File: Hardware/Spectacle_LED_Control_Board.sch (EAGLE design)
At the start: 39 parts, among them J1 FTDI_DEVICE, J10 AUDIO-JACK3, J3 USB-MICROB, J4 AUDIO-JACK3, U1 CY8C4146LQI-S422, U2 3.3V/150mA

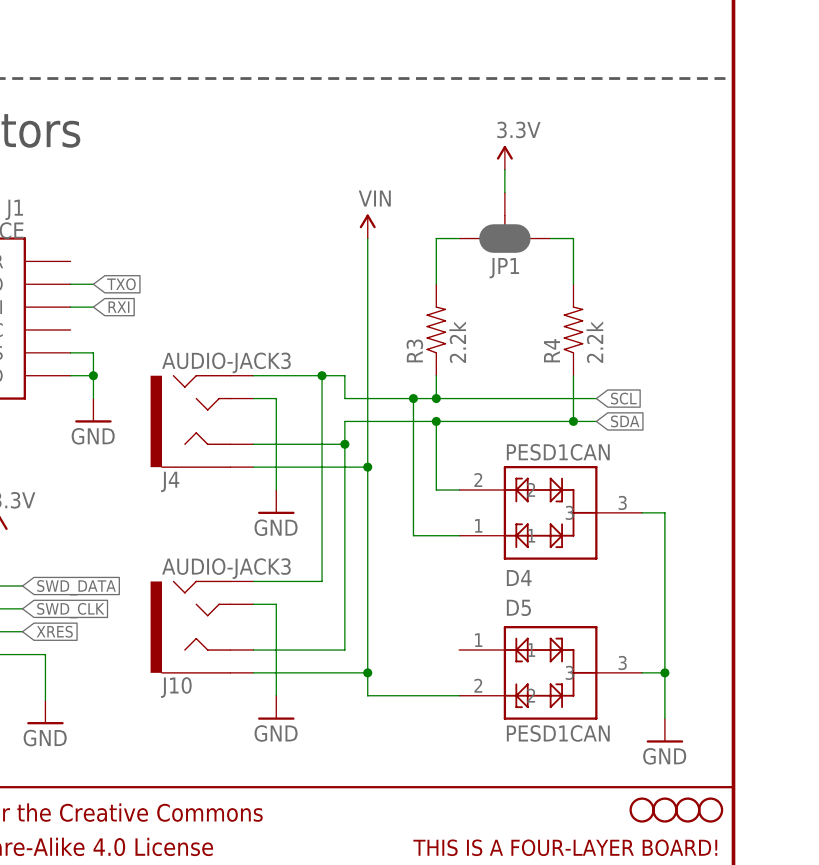
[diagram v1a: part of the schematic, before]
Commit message: QC edits, round one
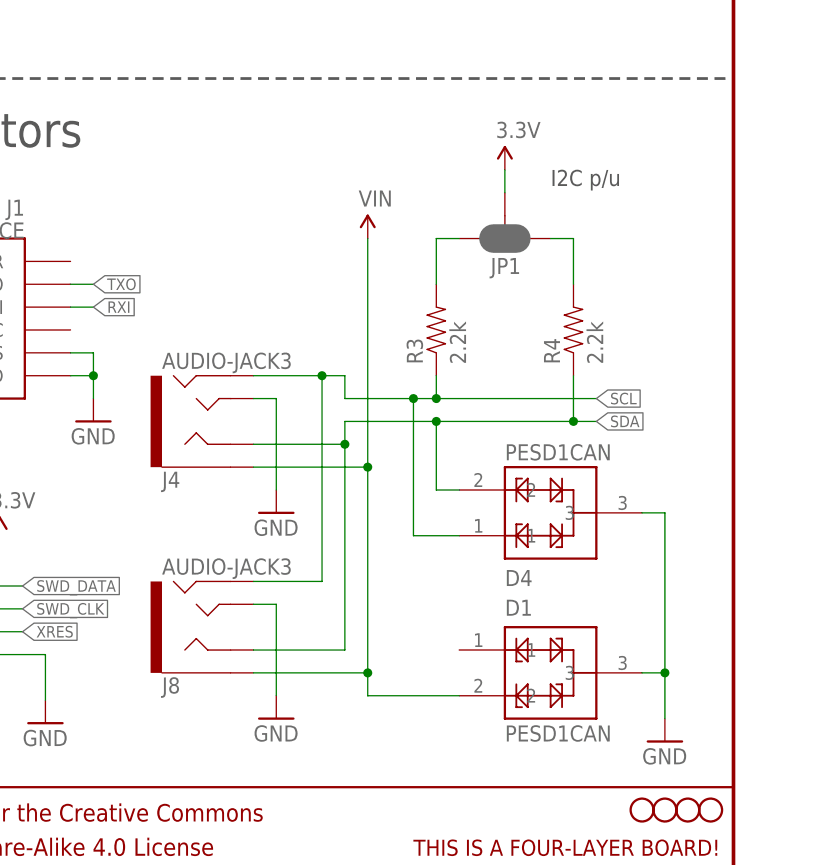
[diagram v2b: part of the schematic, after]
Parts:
- renumbered D5 to D1, J10 to J8
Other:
- note added: "I2C p/u"
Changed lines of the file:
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@@
 <?xml version="1.0" encoding="utf-8"?>
 <!DOCTYPE eagle SYSTEM "eagle.dtd">
-<eagle version="7.3.0">
+<eagle version="7.6.0">
 <drawing>
 <settings>
@@
 <part name="D4" library="SparkFun-DiscreteSemi" deviceset="PESD1CAN" device=""/>
 <part name="GND4" library="SparkFun-Aesthetics" deviceset="GND" device=""/>
-<part name="D5" library="SparkFun-DiscreteSemi" deviceset="PESD1CAN" device=""/>
+<part name="D1" library="SparkFun-DiscreteSemi" deviceset="PESD1CAN" device=""/>
 <part name="SUPPLY1" library="SparkFun-Aesthetics" deviceset="3.3V" device=""/>
 <part name="H1" library="SparkFun-Electromechanical" deviceset="STAND-OFF" device=""/>
@@
 <part name="LOGO1" library="SparkFun-Aesthetics" deviceset="OSHW-LOGO" device="S"/>
 <part name="LOGO2" library="SparkFun-Aesthetics" deviceset="SFE_LOGO_NAME_FLAME" device=".1_INCH"/>
-<part name="J10" library="SparkFun-Connectors" deviceset="AUDIO-JACK3" device=""/>
+<part name="J8" library="SparkFun-Connectors" deviceset="AUDIO-JACK3" device=""/>
 <part name="GND16" library="SparkFun-Aesthetics" deviceset="GND" device=""/>
 <part name="GND17" library="SparkFun-Aesthetics" deviceset="GND" device=""/>
@@
 Supply</text>
 <text x="4.318" y="88.9" size="2.54" layer="97" font="vector">4.5V &lt; VIN &lt; 5.5V</text>
+<text x="228.6" y="102.362" size="1.778" layer="97" font="vector">I2C p/u</text>
 </plain>
 <instances>
@@
 <instance part="D4" gate="G$1" x="223.52" y="71.12" rot="MR180"/>
 <instance part="GND4" gate="1" x="241.3" y="40.64"/>
-<instance part="D5" gate="G$1" x="223.52" y="43.18"/>
+<instance part="D1" gate="G$1" x="223.52" y="43.18"/>
 <instance part="SUPPLY1" gate="G$1" x="22.86" y="177.8"/>
 <instance part="H1" gate="G$1" x="246.38" y="33.02"/>
@@
 <instance part="LOGO1" gate="G$1" x="81.28" y="10.16"/>
 <instance part="LOGO2" gate="G$1" x="88.9" y="0"/>
-<instance part="J10" gate="G$1" x="190.5" y="53.34" rot="MR180"/>
+<instance part="J8" gate="G$1" x="190.5" y="53.34" rot="MR180"/>
 <instance part="GND16" gate="1" x="198.12" y="43.18"/>
 <instance part="GND17" gate="1" x="27.94" y="22.86"/>
@@
 <wire x1="238.76" y1="66.04" x2="241.3" y2="66.04" width="0.1524" layer="91"/>
 <wire x1="241.3" y1="66.04" x2="241.3" y2="48.26" width="0.1524" layer="91"/>
-<pinref part="D5" gate="G$1" pin="3"/>
+<pinref part="D1" gate="G$1" pin="3"/>
 <wire x1="241.3" y1="48.26" x2="241.3" y2="43.18" width="0.1524" layer="91"/>
 <wire x1="238.76" y1="48.26" x2="241.3" y2="48.26" width="0.1524" layer="91"/>
@@
 </segment>
 <segment>
-<pinref part="J10" gate="G$1" pin="TIP"/>
+<pinref part="J8" gate="G$1" pin="TIP"/>
 <pinref part="GND16" gate="1" pin="GND"/>
 <wire x1="195.58" y1="55.88" x2="198.12" y2="55.88" width="0.1524" layer="91"/>
@@
 <wire x1="208.28" y1="45.72" x2="208.28" y2="48.26" width="0.1524" layer="91"/>
 <junction x="208.28" y="71.12"/>
-<pinref part="D5" gate="G$1" pin="2"/>
+<pinref part="D1" gate="G$1" pin="2"/>
 <wire x1="208.28" y1="48.26" x2="208.28" y2="71.12" width="0.1524" layer="91"/>
 <wire x1="208.28" y1="45.72" x2="218.44" y2="45.72" width="0.1524" layer="91"/>
-<pinref part="J10" gate="G$1" pin="EARTH"/>
+<pinref part="J8" gate="G$1" pin="EARTH"/>
 <wire x1="195.58" y1="48.26" x2="208.28" y2="48.26" width="0.1524" layer="91"/>
 <junction x="208.28" y="48.26"/>
@@
 <pinref part="D4" gate="G$1" pin="1"/>
 <wire x1="218.44" y1="63.5" x2="213.36" y2="63.5" width="0.1524" layer="91"/>
-<pinref part="J10" gate="G$1" pin="RING2"/>
+<pinref part="J8" gate="G$1" pin="RING2"/>
 <wire x1="195.58" y1="58.42" x2="203.2" y2="58.42" width="0.1524" layer="91"/>
 <wire x1="203.2" y1="58.42" x2="203.2" y2="81.28" width="0.1524" layer="91"/>
@@
 <wire x1="205.74" y1="73.66" x2="205.74" y2="50.8" width="0.1524" layer="91"/>
 <junction x="205.74" y="73.66"/>
-<pinref part="J10" gate="G$1" pin="RING1"/>
+<pinref part="J8" gate="G$1" pin="RING1"/>
 <wire x1="205.74" y1="50.8" x2="195.58" y2="50.8" width="0.1524" layer="91"/>
 </segment>

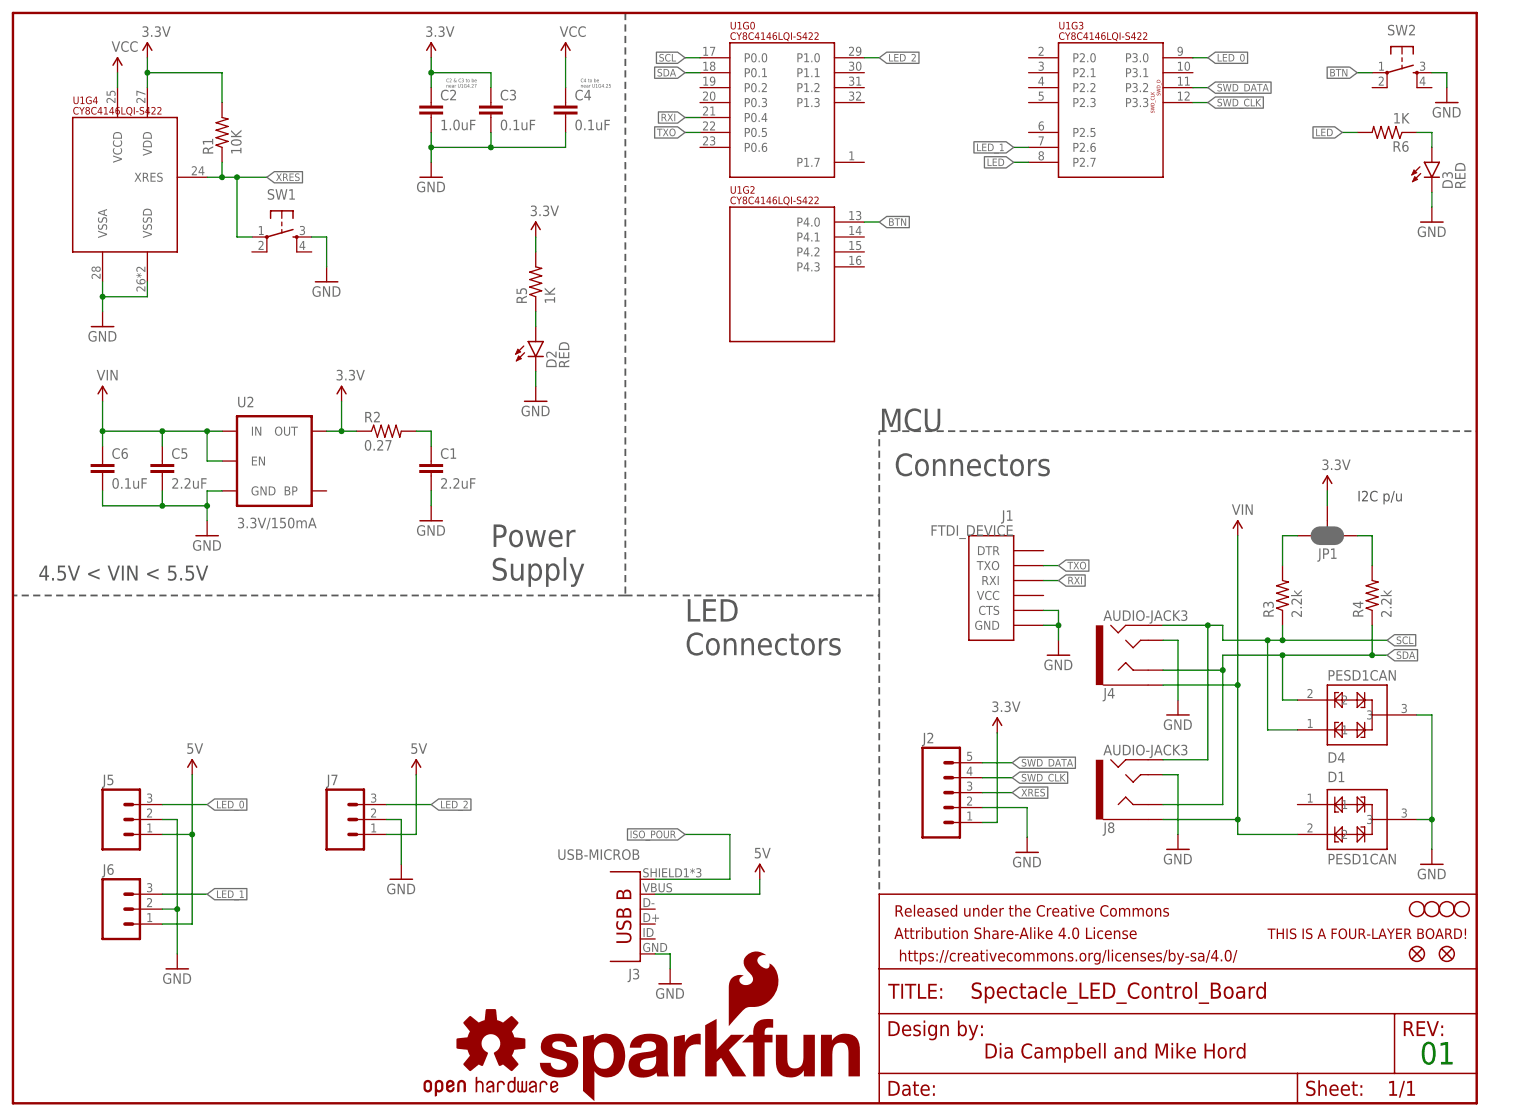
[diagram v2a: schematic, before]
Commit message: Added circuitry for downstream power control
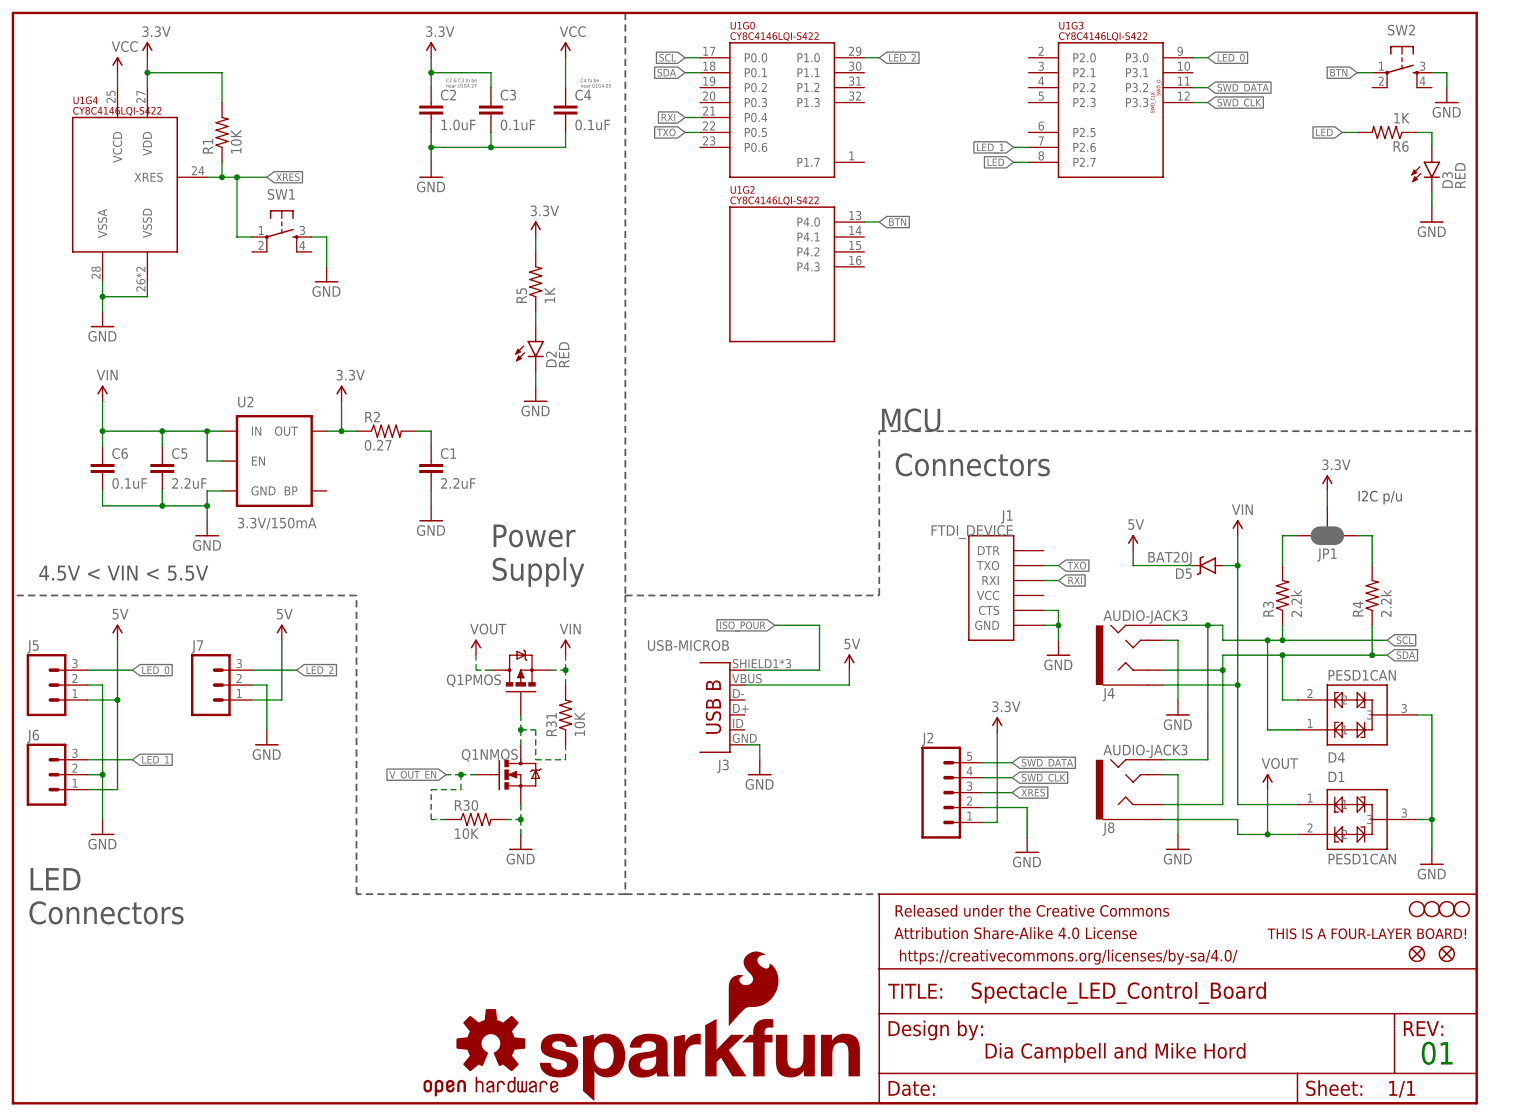
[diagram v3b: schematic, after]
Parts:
- added D5: BAT20J, SparkFun-DiscreteSemi:DIODE-SCHOTTKY-BAT20J
- added Q1: (no value), SparkFun-DiscreteSemi:IRF7509
- added R30, R31: 10K, SparkFun-Resistors:10KOHM-1/10W-1%(0603)0603
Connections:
- new net N$26: Q1NMOS.D, Q1PMOS.G, R31.1
- new net VOUT: D1.2, J8.EARTH, Q1PMOS.D
- new net V_OUT_EN: Q1NMOS.G, R30.1
- net 5V: now also D5.C
- net GND: now also Q1NMOS.S, R30.2
- net VIN: now also D1.1, D5.A, Q1PMOS.S, R31.2; no longer D1.2, J8.EARTH
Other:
- moved on the sheet: J3, J5, J6, J7

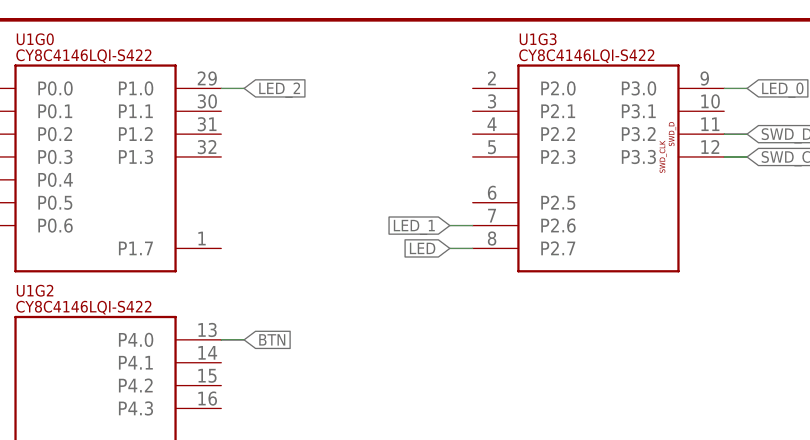
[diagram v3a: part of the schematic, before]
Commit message: Added enable pin
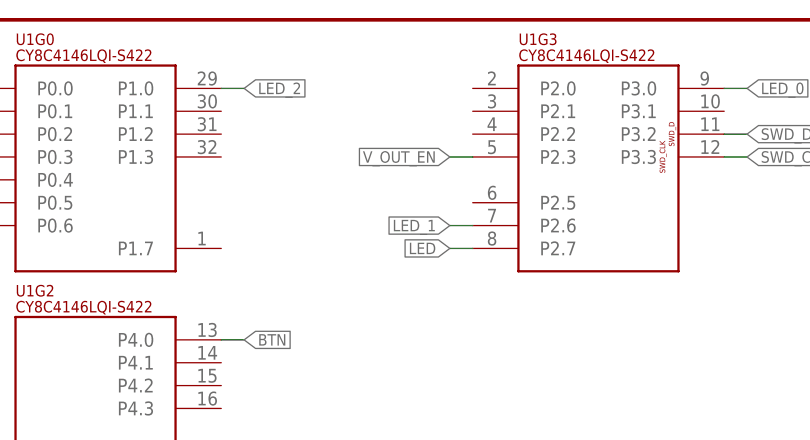
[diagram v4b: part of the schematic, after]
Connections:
- net V_OUT_EN: now also U1G3.P2.3
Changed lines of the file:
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@@
 <junction x="76.2" y="55.88"/>
+</segment>
+<segment>
+<pinref part="U1" gate="G3" pin="P2.3"/>
+<wire x1="172.72" y1="170.18" x2="170.18" y2="170.18" width="0.1524" layer="91"/>
+<label x="170.18" y="170.18" size="1.27" layer="95" rot="R180" xref="yes"/>
 </segment>
 </net>
